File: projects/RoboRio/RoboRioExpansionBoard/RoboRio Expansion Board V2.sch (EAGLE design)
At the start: 97 parts, among them J1 RRINTERFACE-FEMALE, J2 MICROSD, Q1 5.0 MHz, T1 NPN-SOT416, T2 NPN-SOT416, U1 P8X32A-Q44, U2 24LC256ST, U3 FT232RL, U4 MC1525TO, U6 RT9193-33GB, U7 RT9193-33GB

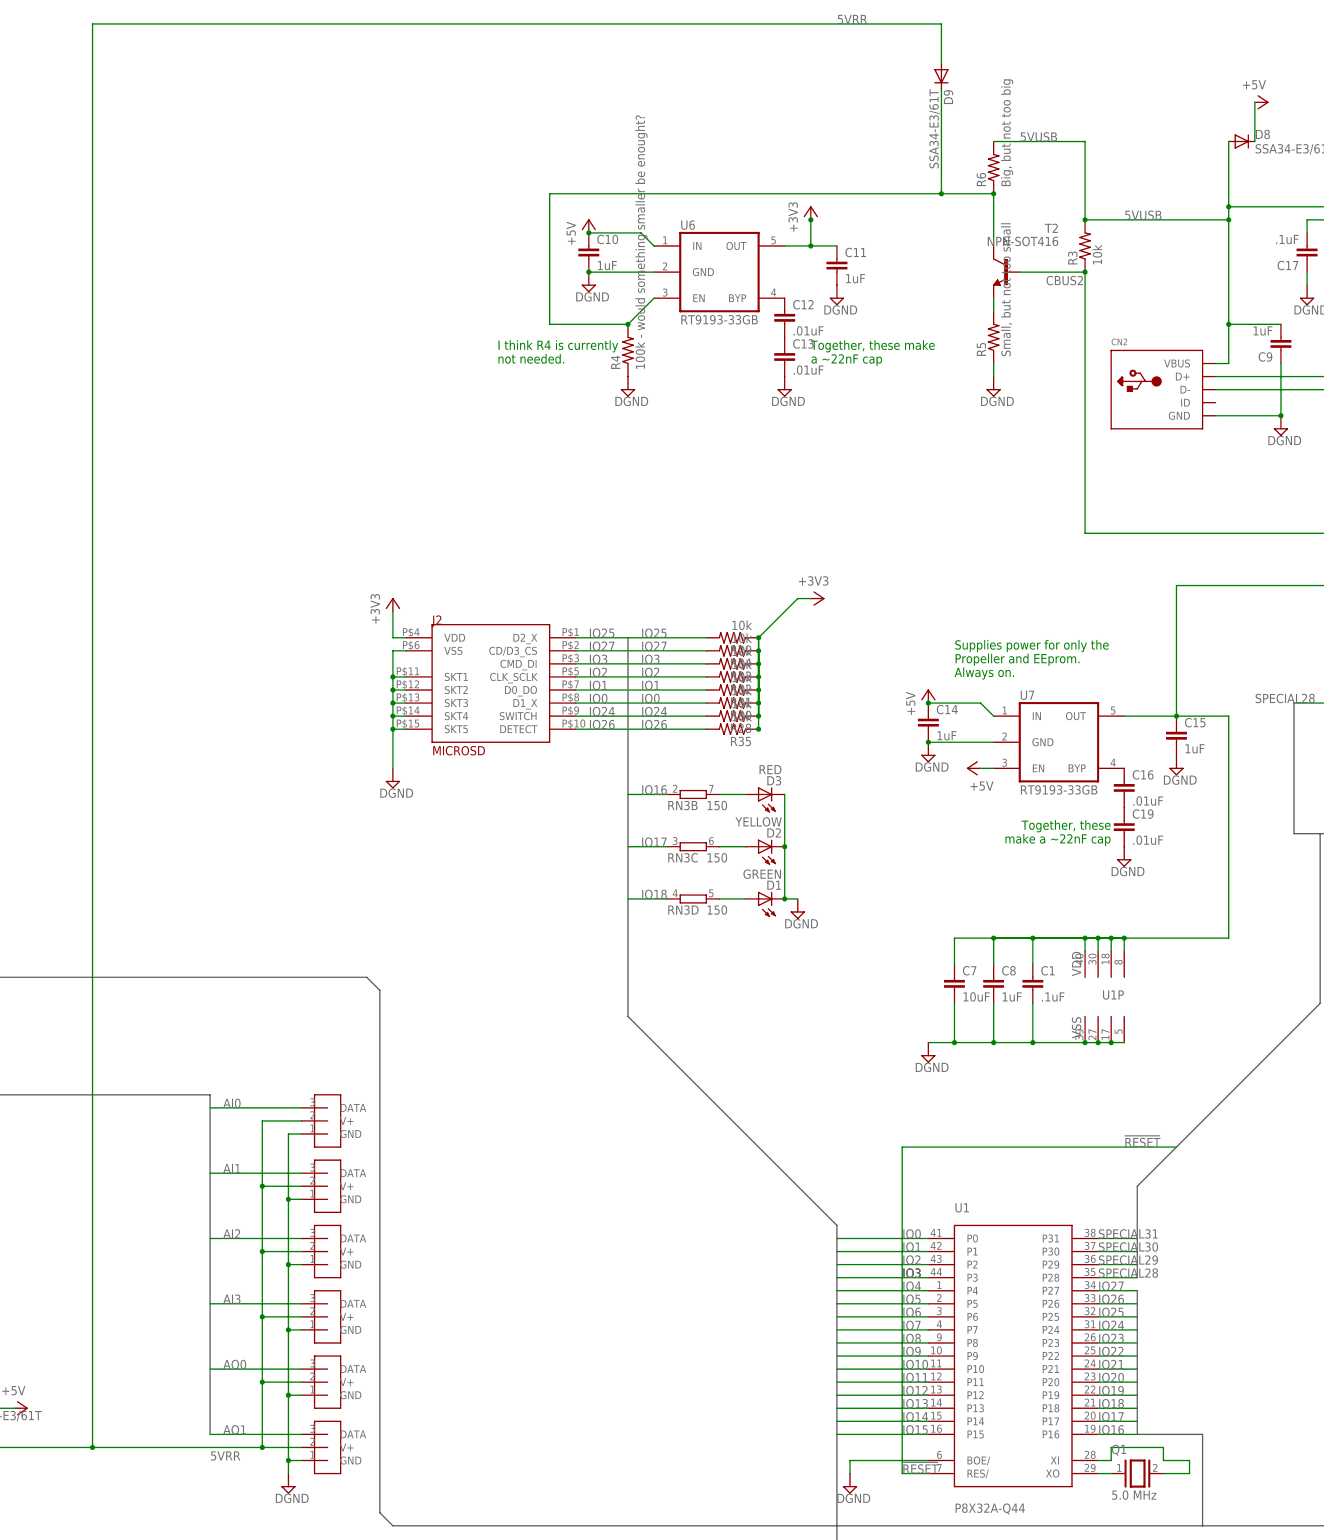
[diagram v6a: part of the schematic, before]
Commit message: Updated power supply thing
Now has real values
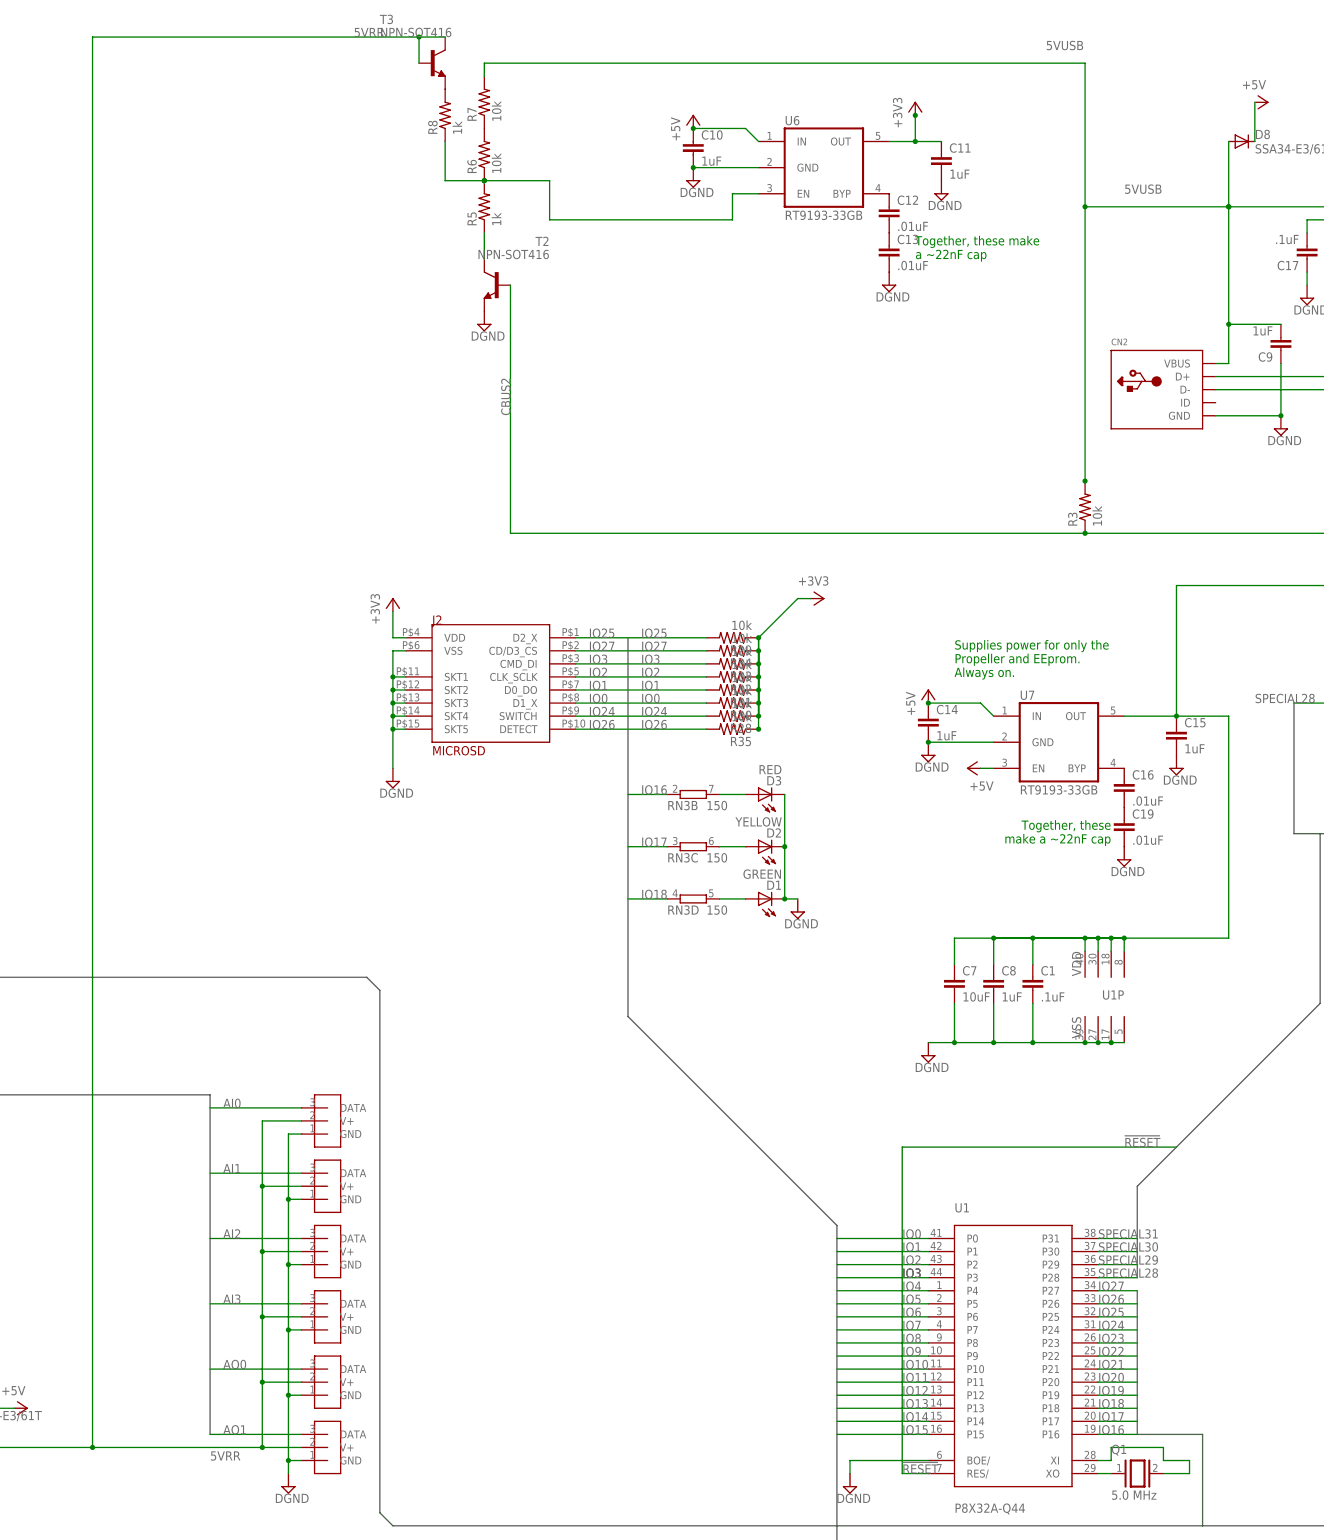
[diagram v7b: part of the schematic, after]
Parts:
- removed D9: SSA34-E3/61T, diode:DIODE-DO-214AC
- removed R4: 100k - would something smaller be enought?, resistor:R-US_R0603
- added R7: 10k, resistor:R-US_R0603
- added R8: 1k, resistor:R-US_R0603
- added T3: NPN-SOT416, NPN transistor:NPN-SOT416
- R5: value Small, but not too small -> 1k
- R6: value Big, but not too big -> 10k
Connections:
- new net N$21: R6.2, R7.1
- new net N$24: R8.2, T3.E
- net 5VRR: now also T3.B, T3.C; no longer D9.A
- net 5VUSB: now also R7.2; no longer R6.2
- net DGND: now also T2.E; no longer R4.1, R5.1
- net N$25: now also R5.2, R8.1; no longer D9.C, R4.2, T2.C
- net N$5: now also R5.1, T2.C; no longer R5.2, T2.E
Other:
- note removed: "I think R4 is currently not needed."
- moved on the sheet: C10, C11, C12, C13, R3, R5, R6, T2, U6

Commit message: 3 pin correction.
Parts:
- removed D8: SSA34-E3/61T, diode:DIODE-DO-214AC
- removed R3, R6, R7: 10k, resistor:R-US_R0603
- removed R5, R8: 1k, resistor:R-US_R0603
- removed T2, T3: NPN-SOT416, NPN transistor:NPN-SOT416
- C18: value 1uF -> 0.01uF
- R27: value 33k -> 10k
- U3: value FT232RL -> FT232RFTR232R; device ftdichip:FT232RL -> FT232R:FT232RFTR232R
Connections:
- net N$28 renamed N$RX
- removed net 5VRR: D4.A, J1.P1-5V, T3.B, T3.C, U$1.V+, U$10.V+, U$11.V+, U$12.V+, U$13.V+, U$14.V+, U$15.V+, U$16.V+, U$2.V+, U$3.V+, U$4.V+, U$5.V+, U$6.V+, U$7.V+, U$8.V+, U$9.V+
- removed net 5VUSB: C9.2, CN2.VBUS, D8.A, R3.2, R7.2, U3.VCC
- removed net CBUS2: R3.1, T2.B, U3.CBUS2
- removed net N$21: R6.2, R7.1
- removed net N$27: D7.A, U3.CBUS0
- new net N$TX: D7.A, U3.CBUS
- net +5V: now also C9.2, U$13.V+, U$14.V+, U$15.V+, U$16.V+, U$3.V+, U$4.V+; no longer D8.C
- net DGND: now also U$1.GND, U$10.GND, U$11.GND, U$12.GND, U$2.GND, U$5.GND, U$6.GND, U$7.GND, U$8.GND, U$9.GND, U3.AGND, U3.GND1, U3.GND2; no longer T2.E, U$1.DATA, U$10.DATA, U$11.DATA, U$12.DATA, U$2.DATA, U$5.DATA, U$6.DATA, U$7.DATA, U$8.DATA, U$9.DATA, U3.GND@1, U3.GND@2, U3.GND@A
- net N$19: now also U3.DTR; no longer U3.!DTR
- net N$24: now also D4.A, J1.P1-5V, U$1.V+, U$10.V+, U$11.V+, U$12.V+, U$2.V+, U$5.V+, U$6.V+, U$7.V+, U$8.V+, U$9.V+; no longer R8.2, T3.E
- net N$25: no longer R5.2, R6.1, R8.1
- net N$5: now also CN2.VBUS, U3.VCC; no longer R5.1, T2.C
- net PWM0: now also U$1.DATA; no longer U$1.GND
- net PWM1: now also U$2.DATA; no longer U$2.GND
- net PWM2: now also U$5.DATA; no longer U$5.GND
- net PWM3: now also U$6.DATA; no longer U$6.GND
- net PWM4: now also U$7.DATA; no longer U$7.GND
- net PWM5: now also U$8.DATA; no longer U$8.GND
- net PWM6: now also U$9.DATA; no longer U$9.GND
- net PWM7: now also U$10.DATA; no longer U$10.GND
- net PWM8: now also U$11.DATA; no longer U$11.GND
- net PWM9: now also U$12.DATA; no longer U$12.GND
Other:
- note added: "Invert then connect to CBUS 2"
- note removed: "Supplies power for only the Propeller and EEprom. Always on."
- moved on the sheet: C10, C11, C12, C13, C17, C18, C9, D5, D6, D7, R1, R2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
